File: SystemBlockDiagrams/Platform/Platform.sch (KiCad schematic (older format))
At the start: 15 parts

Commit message: Add more connectors, leg board
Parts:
- removed J?: Micro-Fit 3.0 Socket Vertical, symbol Connector_Generic:Conn_02x03_Odd_Even
- removed J?: Micro-Fit 3.0 Socket Rt Angle, symbol Connector_Generic:Conn_02x03_Odd_Even
- removed J?: Micro-Fit 3.0 RT Angle, symbol Connector:Conn_01x03_Female
- removed J?: Micro-Fit 3.0 Vertical, symbol Connector:Conn_01x03_Female
- removed J?: Micro-Fit 3.0 RT Angle, symbol Connector_Generic:Conn_02x02_Odd_Even
- removed J?: Micro-Fit 3.0 Vertical, symbol Connector_Generic:Conn_02x02_Odd_Even
- removed SV? (x2): Enfield S2, symbol Stomp:PneumaticServoValve
- added J?: Micro-Fit 3.0 Plug, symbol Connector_Generic:Conn_02x02_Odd_Even
- added J? (x2): Micro-Fit 3.0 Plug, symbol Connector_Generic:Conn_02x03_Odd_Even
- added J? (x2): Micro-Fit 3.0 Plug, symbol Connector:Conn_01x03_Male
- added J? (x2): Hirose 6-Pin Male, symbol Connector:DIN-6
- added J? (x2): Hirose 6-Pin Female, symbol Connector:DIN-6
- added SV? (x2): Enfield S2, symbol Stomp:PneumaticServoValve
- added U? (x2): AngleSensor, symbol Stomp:AngleSensor
- J? (x3): Supplier DigiKey -> Digi-Key
- J?: Suplier DigiKey -> Digi-Key
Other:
- note added: "60 Degree sensor"
- note added: "Curl"
- note added: "Lift"
- note added: "Mating connector is\nHirose HR10A-7P-6S(73) \nDigi-Key HR1588-ND"
- note added: "Micro-Fit Male Pins 26-30AWG, Gold\nMolex 0430310005\nDigi-Key WM3246CT-ND"
- note added: "Microfit Male Pins 20-24AWG, Gold\nMolex 0430310002\nDigi-Key WM1127CT-ND"
- note added: "Replace existing connector with\nHirose HR10A-7R-6P(73) \nDigi-Key HR1596-ND"
- note added: "S2 to Board Cable\nMcMaster 75985K52"
- note added: "Swing"
- note removed: "Cable\nMcMaster 75985K52"
- note removed: "Mating connector is\nHirose HR10A-7P-6S(73) \nDigiKey HR1588-ND"
- note removed: "Pins 20-24AWG, Gold\nMolex 0430310002\nDigiKey WM1127CT-ND"
- note removed: "Replace exiting connector with\nHirose HR10A-7R-6P(73) \nDigiKey HR1596-ND"
- moved on the sheet: J?, SV?, U?

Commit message: Connector updates
Change S2 cable to pre-made set
Add power connectors
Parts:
- removed J? (x3): Hirose 6-Pin Male, symbol Connector:DIN-6
- removed J? (x3): Hirose 6-Pin Female, symbol Connector:DIN-6
- added J? (x3): M8 5 Pin, symbol Connector:DIN-5
- added J?: Micro-Fit 3.0 Plug, symbol Connector_Generic:Conn_01x02
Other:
- note added: "Comes with 6ft cable"
- note added: "Comms\n26AWG 4 conductor\nCooner Wire NMEF 4/26-6544 J"
- note added: "Power\n20AWG 2 Conductor\nCooner Wire NMEF 2/20-25944 J"
- note added: "Sensor cable is\n26AWG 3 conductor\nCooner Wire NMEF 3/26-6544 J"
- note removed: "Mating connector is\nHirose HR10A-7P-6S(73) \nDigi-Key HR1588-ND"
- note removed: "Replace existing connector with\nHirose HR10A-7R-6P(73) \nDigi-Key HR1596-ND"
- note removed: "S2 to Board Cable\nMcMaster 75985K52"
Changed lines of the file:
@@
 	-1   0    0    -1
 $EndComp
-Text Notes 2150 800  0    50   ~ 0
-Replace existing connector with\nHirose HR10A-7R-6P(73) \nDigi-Key HR1596-ND
-Text Notes 3500 800  0    50   ~ 0
-Mating connector is\nHirose  HR10A-7P-6S(73) \nDigi-Key HR1588-ND
-$Comp
-L Connector:DIN-6 J?
-U 1 1 5E1C5E68
-P 2500 1450
-F 0 "J?" H 2500 2021 50  0000 C CNN
-F 1 "Hirose 6-Pin Male" H 2500 1930 50  0000 C CNN
-F 2 "" H 2500 1450 50  0001 C CNN
-F 3 "https://www.digikey.com/product-detail/en/hirose-electric-co-ltd/HR10A-7R-6P-73/HR1596-ND/1095454" H 2500 1450 50  0001 C CNN
-F 4 "Hirose" H 2500 1450 50  0001 C CNN "Manufaturer"
-F 5 "HR10A-7R-6P(73)" H 2500 1450 50  0001 C CNN "Manufacturer Part Number"
-F 6 "Digi-Key" H 2500 1450 50  0001 C CNN "Supplier"
-F 7 "HR1596-ND" H 2500 1839 50  0000 C CNN "Supplier Part Number"
-	1    2500 1450
-	1    0    0    -1
-$EndComp
-$Comp
-L Connector:DIN-6 J?
-U 1 1 5E1C7296
-P 3850 1450
-F 0 "J?" H 3850 2021 50  0000 C CNN
-F 1 "Hirose 6-Pin Female" H 3850 1930 50  0000 C CNN
-F 2 "" H 3850 1450 50  0001 C CNN
-F 3 "https://www.digikey.com/product-detail/en/hirose-electric-co-ltd/HR10A-7P-6S-73/HR1588-ND/1095446" H 3850 1450 50  0001 C CNN
-F 4 "Hirose" H 3850 1450 50  0001 C CNN "Manufaturer"
-F 5 "HR10A-7R-6S(73)" H 3850 1450 50  0001 C CNN "Manufacturer Part Number"
-F 6 "Digi-Key" H 3850 1450 50  0001 C CNN "Supplier"
-F 7 "HR1588-ND" H 3850 1839 50  0000 C CNN "Supplier Part Number"
-	1    3850 1450
-	1    0    0    -1
-$EndComp
-Text Notes 4700 750  0    50   ~ 0
-S2 to Board Cable\nMcMaster 75985K52
 $Comp
 L Connector_Generic:Conn_02x03_Odd_Even J?
@@
 F 5 "0436400301" H 7050 2050 50  0001 C CNN "Manufacturer Part Number"
 F 6 "Digi-Key" H 7050 2050 50  0001 C CNN "Suplier"
-F 7 " WM1856-ND " H 7050 2050 50  0001 C CNN "Supplier Part Number"
+F 7 " WM1856-ND " H 7150 1850 50  0000 C CNN "Supplier Part Number"
 	1    7050 2050
 	1    0    0    -1
@@
 F8 "CommB" I R 10300 6000 50
 F9 "CommA" I R 10300 1000 50
+F10 "Power" I L 7800 5750 50
 $EndSheet
 $Comp
@@
 $EndComp
 $Comp
-L Connector:DIN-6 J?
-U 1 1 5E21AB4C
-P 2500 2900
-F 0 "J?" H 2500 3471 50  0000 C CNN
-F 1 "Hirose 6-Pin Male" H 2500 3380 50  0000 C CNN
-F 2 "" H 2500 2900 50  0001 C CNN
-F 3 "https://www.digikey.com/product-detail/en/hirose-electric-co-ltd/HR10A-7R-6P-73/HR1596-ND/1095454" H 2500 2900 50  0001 C CNN
-F 4 "Hirose" H 2500 2900 50  0001 C CNN "Manufaturer"
-F 5 "HR10A-7R-6P(73)" H 2500 2900 50  0001 C CNN "Manufacturer Part Number"
-F 6 "Digi-Key" H 2500 2900 50  0001 C CNN "Supplier"
-F 7 "HR1596-ND" H 2500 3289 50  0000 C CNN "Supplier Part Number"
-	1    2500 2900
-	1    0    0    -1
-$EndComp
-$Comp
-L Connector:DIN-6 J?
-U 1 1 5E21AB5A
-P 3850 2900
-F 0 "J?" H 3850 3471 50  0000 C CNN
-F 1 "Hirose 6-Pin Female" H 3850 3380 50  0000 C CNN
-F 2 "" H 3850 2900 50  0001 C CNN
-F 3 "https://www.digikey.com/product-detail/en/hirose-electric-co-ltd/HR10A-7P-6S-73/HR1588-ND/1095446" H 3850 2900 50  0001 C CNN
-F 4 "Hirose" H 3850 2900 50  0001 C CNN "Manufaturer"
-F 5 "HR10A-7R-6S(73)" H 3850 2900 50  0001 C CNN "Manufacturer Part Number"
-F 6 "Digi-Key" H 3850 2900 50  0001 C CNN "Supplier"
-F 7 "HR1588-ND" H 3850 3289 50  0000 C CNN "Supplier Part Number"
-	1    3850 2900
-	1    0    0    -1
-$EndComp
-$Comp
-L Connector:DIN-6 J?
-U 1 1 5E21D03E
-P 2500 4350
-F 0 "J?" H 2500 4921 50  0000 C CNN
-F 1 "Hirose 6-Pin Male" H 2500 4830 50  0000 C CNN
-F 2 "" H 2500 4350 50  0001 C CNN
-F 3 "https://www.digikey.com/product-detail/en/hirose-electric-co-ltd/HR10A-7R-6P-73/HR1596-ND/1095454" H 2500 4350 50  0001 C CNN
-F 4 "Hirose" H 2500 4350 50  0001 C CNN "Manufaturer"
-F 5 "HR10A-7R-6P(73)" H 2500 4350 50  0001 C CNN "Manufacturer Part Number"
-F 6 "Digi-Key" H 2500 4350 50  0001 C CNN "Supplier"
-F 7 "HR1596-ND" H 2500 4739 50  0000 C CNN "Supplier Part Number"
-	1    2500 4350
-	1    0    0    -1
-$EndComp
-$Comp
-L Connector:DIN-6 J?
-U 1 1 5E21D04C
-P 3850 4350
-F 0 "J?" H 3850 4921 50  0000 C CNN
-F 1 "Hirose 6-Pin Female" H 3850 4830 50  0000 C CNN
-F 2 "" H 3850 4350 50  0001 C CNN
-F 3 "https://www.digikey.com/product-detail/en/hirose-electric-co-ltd/HR10A-7P-6S-73/HR1588-ND/1095446" H 3850 4350 50  0001 C CNN
-F 4 "Hirose" H 3850 4350 50  0001 C CNN "Manufaturer"
-F 5 "HR10A-7R-6S(73)" H 3850 4350 50  0001 C CNN "Manufacturer Part Number"
-F 6 "Digi-Key" H 3850 4350 50  0001 C CNN "Supplier"
-F 7 "HR1588-ND" H 3850 4739 50  0000 C CNN "Supplier Part Number"
-	1    3850 4350
-	1    0    0    -1
-$EndComp
+L Connector:DIN-5 J?
+U 1 1 5E24883E
+P 2600 1250
+F 0 "J?" H 2600 975 50  0000 C CNN
+F 1 "M8 5 Pin" H 2600 884 50  0000 C CNN
+F 2 "" H 2600 1250 50  0001 C CNN
+F 3 "https://www.mcmaster.com/7138k39" H 2600 1250 50  0001 C CNN
+F 4 "McMaster-Carr" H 2600 1250 50  0001 C CNN "Supplier"
+F 5 "7138K39" H 2600 1250 50  0001 C CNN "Supplier Part Number"
+	1    2600 1250
+	1    0    0    -1
+$EndComp
+$Comp
+L Connector:DIN-5 J?
+U 1 1 5E2490C7
+P 2600 2700
+F 0 "J?" H 2600 2425 50  0000 C CNN
+F 1 "M8 5 Pin" H 2600 2334 50  0000 C CNN
+F 2 "" H 2600 2700 50  0001 C CNN
+F 3 "https://www.mcmaster.com/7138k39" H 2600 2700 50  0001 C CNN
+F 4 "McMaster-Carr" H 2600 2700 50  0001 C CNN "Supplier"
+F 5 "7138K39" H 2600 2700 50  0001 C CNN "Supplier Part Number"
+	1    2600 2700
+	1    0    0    -1
+$EndComp
+$Comp
+L Connector:DIN-5 J?
+U 1 1 5E24A55F
+P 2600 4150
+F 0 "J?" H 2600 3875 50  0000 C CNN
+F 1 "M8 5 Pin" H 2600 3784 50  0000 C CNN
+F 2 "" H 2600 4150 50  0001 C CNN
+F 3 "https://www.mcmaster.com/7138k39" H 2600 4150 50  0001 C CNN
+F 4 "McMaster-Carr" H 2600 4150 50  0001 C CNN "Supplier"
+F 5 "7138K39" H 2600 4150 50  0001 C CNN "Supplier Part Number"
+	1    2600 4150
+	1    0    0    -1
+$EndComp
+Text Notes 3050 1250 0    50   ~ 0
+Comes with 6ft cable
+Text Notes 4700 3500 0    50   ~ 0
+Sensor cable is\n26AWG 3 conductor\nCooner Wire NMEF 3/26-6544 J
+Text Notes 10900 4450 1    50   ~ 0
+Comms\n26AWG 4 conductor\nCooner Wire NMEF 4/26-6544 J
+Text Notes 5400 6000 0    50   ~ 0
+Power\n20AWG 2 Conductor\nCooner Wire NMEF 2/20-25944 J
+$Comp
+L Connector_Generic:Conn_01x02 J?
+U 1 1 5E24D156
+P 7100 5800
+F 0 "J?" H 7180 5837 50  0000 L CNN
+F 1 "Micro-Fit 3.0 Plug" H 7180 5746 50  0000 L CNN
+F 2 "" H 7100 5800 50  0001 C CNN
+F 3 "https://www.digikey.com/product-detail/en/molex/0436450208/WM11226-ND/4247418" H 7100 5800 50  0001 C CNN
+F 4 "WM10658-ND" H 7180 5655 50  0000 L CNN "Supplier part Number"
+F 5 "Digi-Key" H 7100 5800 50  0001 C CNN "Supplier"
+F 6 "Molex" H 7100 5800 50  0001 C CNN "manufacturer"
+F 7 "0436450208" H 7100 5800 50  0001 C CNN "Manufacturer part Number"
+	1    7100 5800
+	1    0    0    -1
+$EndComp

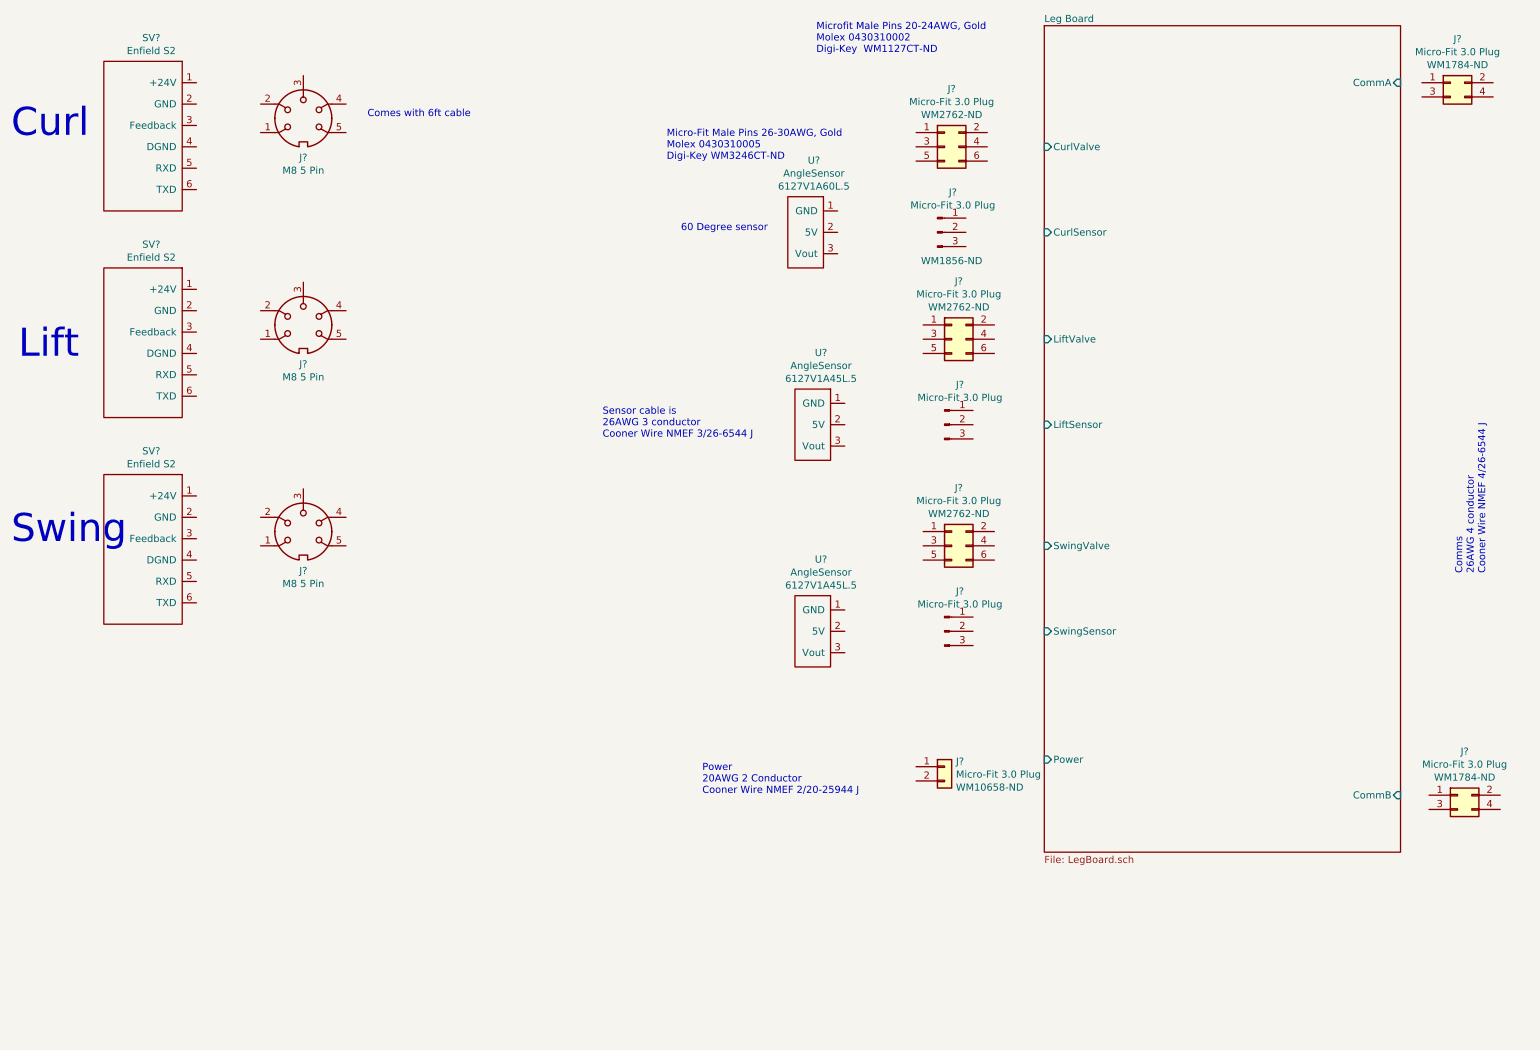
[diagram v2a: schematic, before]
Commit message: Switch Leg Board connectors
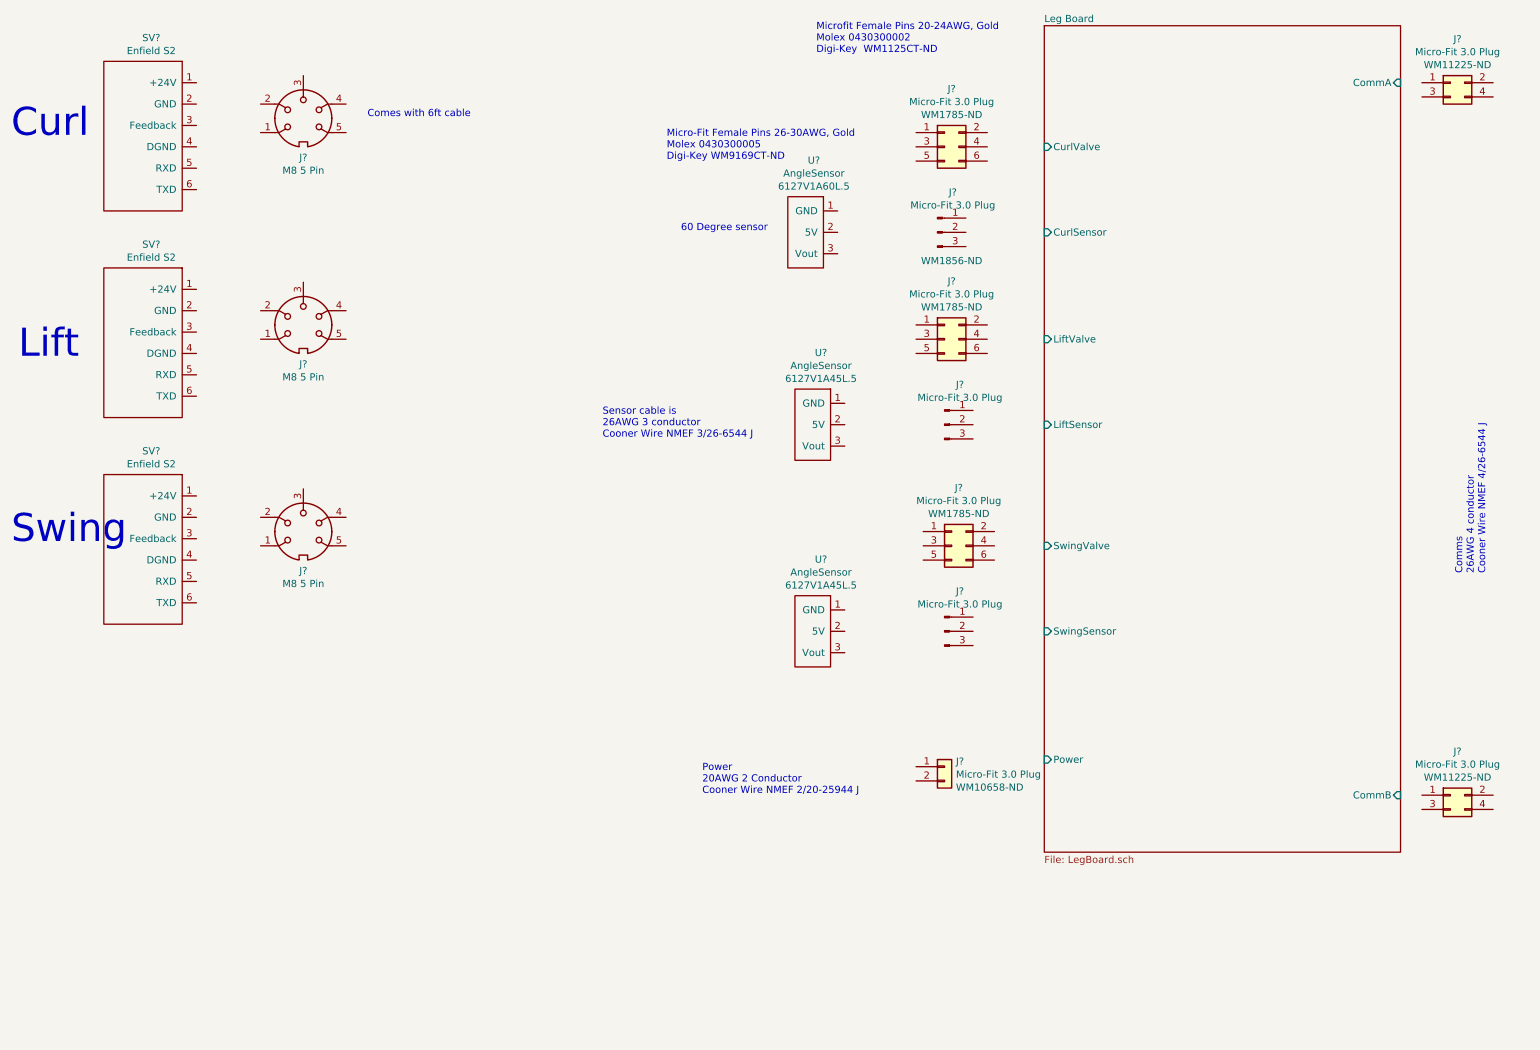
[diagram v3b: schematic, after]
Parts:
- removed J?: Micro-Fit 3.0 Plug, symbol Connector_Generic:Conn_02x02_Odd_Even
- removed J? (x2): Micro-Fit 3.0 Plug, symbol Connector_Generic:Conn_02x03_Odd_Even
- added J? (x2): Micro-Fit 3.0 Plug, symbol Connector_Generic:Conn_02x03_Odd_Even
- added J?: Micro-Fit 3.0 Plug, symbol Connector_Generic:Conn_02x02_Odd_Even
- J?: Manufacturer (none) -> Molex; Manufacturer Part Number (none) -> 0430250600; Supplier Part Number WM2762-ND -> WM1785-ND
- J?: Manufacturer part Number 0430250400 -> 0430250408; Supplier Part Number WM1784-ND -> WM11225-ND
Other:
- note added: "Micro-Fit Female Pins 26-30AWG, Gold\nMolex 0430300005\nDigi-Key WM9169CT-ND"
- note added: "Microfit Female Pins 20-24AWG, Gold\nMolex 0430300002\nDigi-Key WM1125CT-ND"
- note removed: "Micro-Fit Male Pins 26-30AWG, Gold\nMolex 0430310005\nDigi-Key WM3246CT-ND"
- note removed: "Microfit Male Pins 20-24AWG, Gold\nMolex 0430310002\nDigi-Key WM1127CT-ND"
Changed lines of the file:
@@
 F 1 "Micro-Fit 3.0 Plug" H 7150 1766 50  0000 C CNN
 F 2 "" H 7100 1450 50  0001 C CNN
-F 3 "https://www.digikey.com/product-detail/en/molex/0430200601/WM2762-ND/1132438" H 7100 1450 50  0001 C CNN
+F 3 "https://www.digikey.com/product-detail/en/molex/0430250600/WM1785-ND/252498" H 7100 1450 50  0001 C CNN
 F 4 "Digi-Key" H 7100 1450 50  0001 C CNN "Supplier"
-F 5 " WM2762-ND " H 7150 1675 50  0000 C CNN "Supplier Part Number"
+F 5 "WM1785-ND " H 7150 1675 50  0000 C CNN "Supplier Part Number"
+F 6 "Molex" H 7100 1450 50  0001 C CNN "Manufacturer"
+F 7 "0430250600" H 7100 1450 50  0001 C CNN "Manufacturer Part Number"
 	1    7100 1450
 	1    0    0    -1
 $EndComp
 Text Notes 6200 800  0    50   ~ 0
-Microfit Male Pins 20-24AWG, Gold\nMolex 0430310002\nDigi-Key  WM1127CT-ND
+Microfit Female Pins 20-24AWG, Gold\nMolex 0430300002\nDigi-Key  WM1125CT-ND
 $Comp
 L Connector:Conn_01x03_Male J?
@@
 F 1 "Micro-Fit 3.0 Plug" H 10700 1216 50  0000 C CNN
 F 2 "" H 10650 1000 50  0001 C CNN
-F 3 "https://www.digikey.com/product-detail/en/molex/0430250400/WM1784-ND/252497" H 10650 1000 50  0001 C CNN
+F 3 "https://www.digikey.com/product-detail/en/molex/0430250408/WM11225-ND/4481508" H 10650 1000 50  0001 C CNN
 F 4 "DigiKey" H 10650 1000 50  0001 C CNN "Supplier"
-F 5 "WM1784-ND" H 10700 1125 50  0000 C CNN "Supplier Part Number"
+F 5 "WM11225-ND" H 10700 1125 50  0000 C CNN "Supplier Part Number"
 F 6 "Molex" H 10650 1000 50  0001 C CNN "Manufacturer"
-F 7 "0430250400" H 10650 1000 50  0001 C CNN "Manufacturer part Number"
+F 7 "0430250408" H 10650 1000 50  0001 C CNN "Manufacturer part Number"
 	1    10650 1000
 	1    0    0    -1
@@
 $EndSheet
 $Comp
-L Connector_Generic:Conn_02x02_Odd_Even J?
-U 1 1 5E1D8173
-P 10700 6000
-F 0 "J?" H 10750 6307 50  0000 C CNN
-F 1 "Micro-Fit 3.0 Plug" H 10750 6216 50  0000 C CNN
-F 2 "" H 10700 6000 50  0001 C CNN
-F 3 "https://www.digikey.com/product-detail/en/molex/0430250400/WM1784-ND/252497" H 10700 6000 50  0001 C CNN
-F 4 "DigiKey" H 10700 6000 50  0001 C CNN "Supplier"
-F 5 "WM1784-ND" H 10750 6125 50  0000 C CNN "Supplier Part Number"
-F 6 "Molex" H 10700 6000 50  0001 C CNN "Manufacturer"
-F 7 "0430250400" H 10700 6000 50  0001 C CNN "Manufacturer part Number"
-	1    10700 6000
-	1    0    0    -1
-$EndComp
-$Comp
 L Stomp:AngleSensor U?
 U 1 1 5E1C2B3D
@@
 $EndComp
 Text Notes 5150 1550 0    50   ~ 0
-Micro-Fit Male Pins 26-30AWG, Gold\nMolex 0430310005\nDigi-Key WM3246CT-ND
-$Comp
-L Connector_Generic:Conn_02x03_Odd_Even J?
-U 1 1 5E216DD2
-P 7150 2800
-F 0 "J?" H 7200 3207 50  0000 C CNN
-F 1 "Micro-Fit 3.0 Plug" H 7200 3116 50  0000 C CNN
-F 2 "" H 7150 2800 50  0001 C CNN
-F 3 "https://www.digikey.com/product-detail/en/molex/0430200601/WM2762-ND/1132438" H 7150 2800 50  0001 C CNN
-F 4 "Digi-Key" H 7150 2800 50  0001 C CNN "Supplier"
-F 5 " WM2762-ND " H 7200 3025 50  0000 C CNN "Supplier Part Number"
-	1    7150 2800
-	1    0    0    -1
-$EndComp
+Micro-Fit Female Pins 26-30AWG, Gold\nMolex 0430300005\nDigi-Key WM9169CT-ND
 $Comp
 L Connector:Conn_01x03_Male J?
@@
 $EndComp
 $Comp
-L Connector_Generic:Conn_02x03_Odd_Even J?
-U 1 1 5E2191A0
-P 7150 4250
-F 0 "J?" H 7200 4657 50  0000 C CNN
-F 1 "Micro-Fit 3.0 Plug" H 7200 4566 50  0000 C CNN
-F 2 "" H 7150 4250 50  0001 C CNN
-F 3 "https://www.digikey.com/product-detail/en/molex/0430200601/WM2762-ND/1132438" H 7150 4250 50  0001 C CNN
-F 4 "Digi-Key" H 7150 4250 50  0001 C CNN "Supplier"
-F 5 " WM2762-ND " H 7200 4475 50  0000 C CNN "Supplier Part Number"
-	1    7150 4250
-	1    0    0    -1
-$EndComp
-$Comp
 L Connector:Conn_01x03_Male J?
 U 1 1 5E2191AE
@@
 	1    0    0    -1
 $EndComp
+$Comp
+L Connector_Generic:Conn_02x03_Odd_Even J?
+U 1 1 5E24439A
+P 7100 2800
+F 0 "J?" H 7150 3207 50  0000 C CNN
+F 1 "Micro-Fit 3.0 Plug" H 7150 3116 50  0000 C CNN
+F 2 "" H 7100 2800 50  0001 C CNN
+F 3 "https://www.digikey.com/product-detail/en/molex/0430250600/WM1785-ND/252498" H 7100 2800 50  0001 C CNN
+F 4 "Digi-Key" H 7100 2800 50  0001 C CNN "Supplier"
+F 5 "WM1785-ND " H 7150 3025 50  0000 C CNN "Supplier Part Number"
+F 6 "Molex" H 7100 2800 50  0001 C CNN "Manufacturer"
+F 7 "0430250600" H 7100 2800 50  0001 C CNN "Manufacturer Part Number"
+	1    7100 2800
+	1    0    0    -1
+$EndComp
+$Comp
+L Connector_Generic:Conn_02x03_Odd_Even J?
+U 1 1 5E244DE8
+P 7150 4250
+F 0 "J?" H 7200 4657 50  0000 C CNN
+F 1 "Micro-Fit 3.0 Plug" H 7200 4566 50  0000 C CNN
+F 2 "" H 7150 4250 50  0001 C CNN
+F 3 "https://www.digikey.com/product-detail/en/molex/0430250600/WM1785-ND/252498" H 7150 4250 50  0001 C CNN
+F 4 "Digi-Key" H 7150 4250 50  0001 C CNN "Supplier"
+F 5 "WM1785-ND " H 7200 4475 50  0000 C CNN "Supplier Part Number"
+F 6 "Molex" H 7150 4250 50  0001 C CNN "Manufacturer"
+F 7 "0430250600" H 7150 4250 50  0001 C CNN "Manufacturer Part Number"
+	1    7150 4250
+	1    0    0    -1
+$EndComp
+$Comp
+L Connector_Generic:Conn_02x02_Odd_Even J?
+U 1 1 5E245917
+P 10650 6000
+F 0 "J?" H 10700 6307 50  0000 C CNN
+F 1 "Micro-Fit 3.0 Plug" H 10700 6216 50  0000 C CNN
+F 2 "" H 10650 6000 50  0001 C CNN
+F 3 "https://www.digikey.com/product-detail/en/molex/0430250408/WM11225-ND/4481508" H 10650 6000 50  0001 C CNN
+F 4 "DigiKey" H 10650 6000 50  0001 C CNN "Supplier"
+F 5 "WM11225-ND" H 10700 6125 50  0000 C CNN "Supplier Part Number"
+F 6 "Molex" H 10650 6000 50  0001 C CNN "Manufacturer"
+F 7 "0430250408" H 10650 6000 50  0001 C CNN "Manufacturer part Number"
+	1    10650 6000
+	1    0    0    -1
+$EndComp
